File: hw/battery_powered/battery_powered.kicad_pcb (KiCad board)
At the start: 2 copper layers, 69.4 x 54 mm, 10 parts, among them SW101 SKRPABE010, SW102 SKRPABE010, U102 OSL10564-IB, U103 chofutech_logo

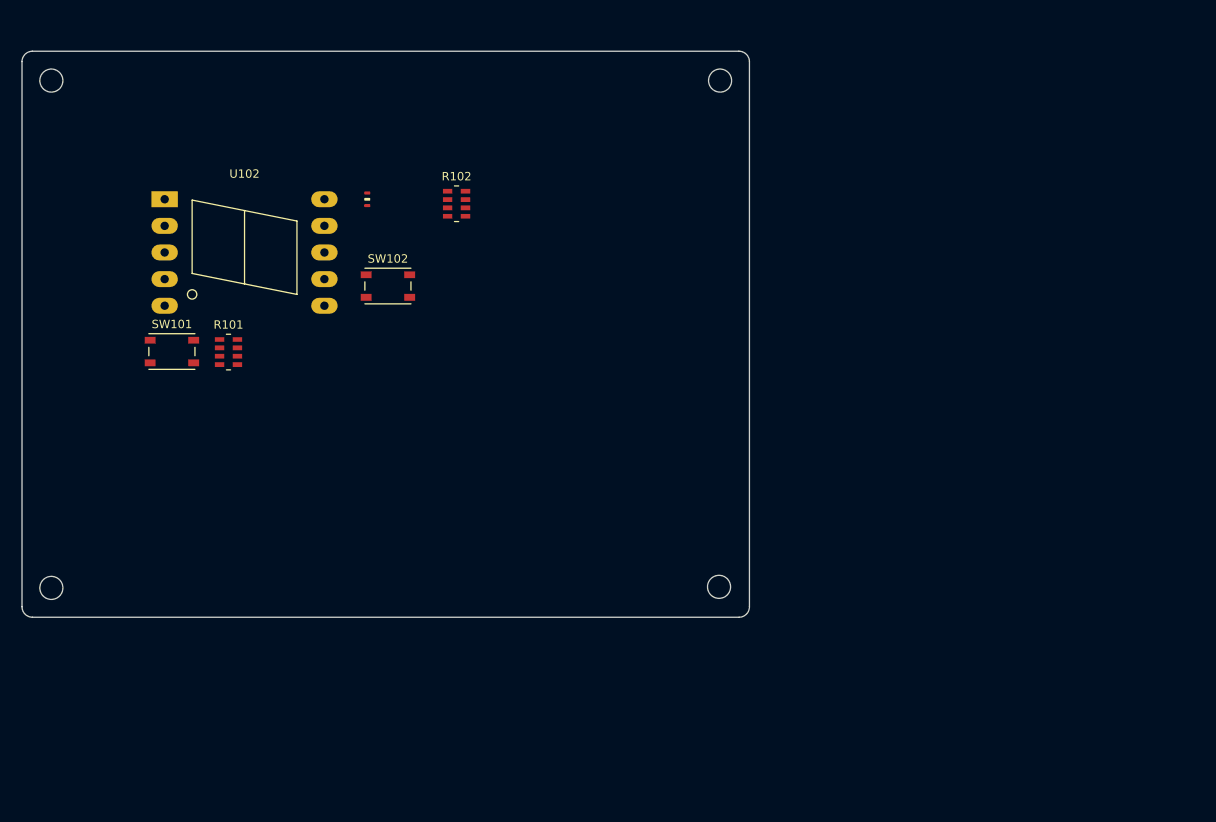
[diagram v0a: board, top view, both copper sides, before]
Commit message: add battery_powered footprints
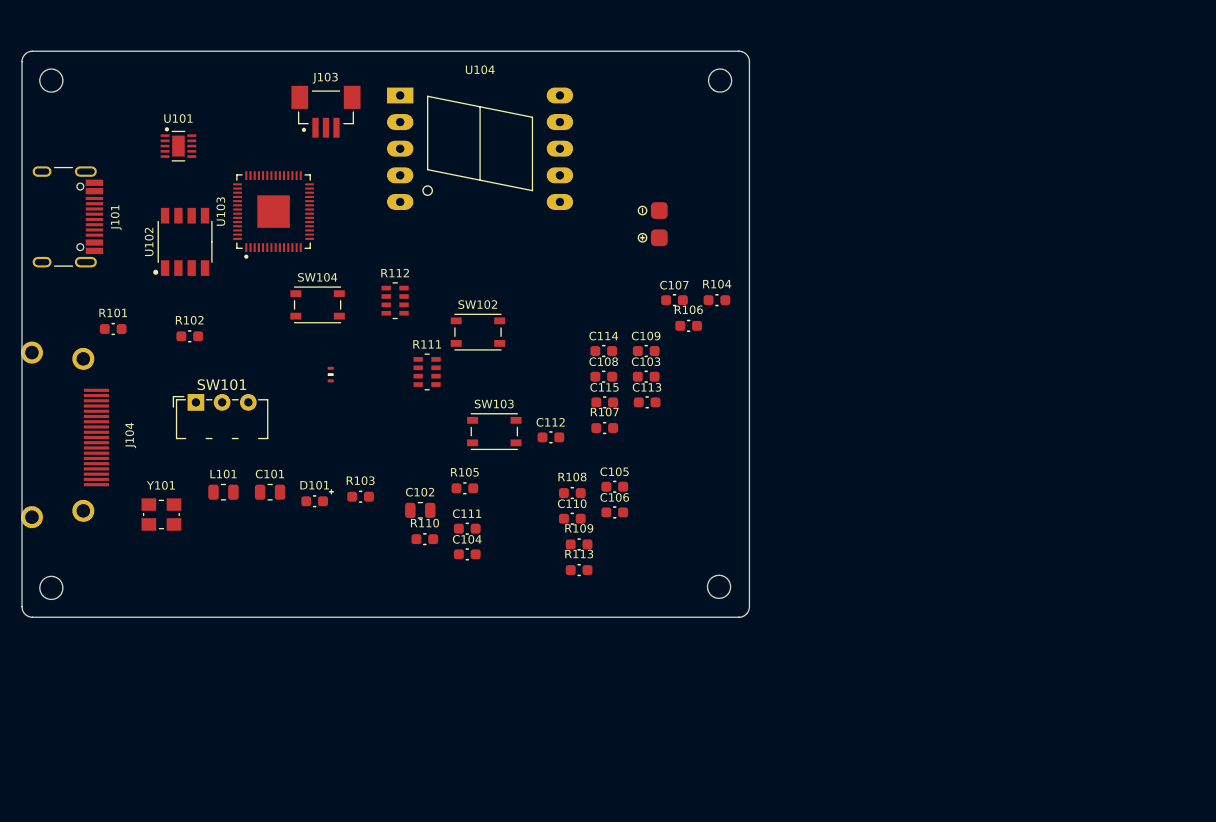
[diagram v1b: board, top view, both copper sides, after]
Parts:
- added C101: C_2012m, 00_custom_lib:C_2012m, F.Cu at (73.7, 92.1)
- added C102: C_2012m, 00_custom_lib:C_2012m, F.Cu at (88.0, 93.8)
- added C103: C_1608m, 00_custom_lib:C_1608m, F.Cu at (109.5, 81.0)
- added C104: C_1608m, 00_custom_lib:C_1608m, F.Cu at (92.5, 98.0)
- added C105: C_1608m, 00_custom_lib:C_1608m, F.Cu at (106.5, 91.5)
- added C106: C_1608m, 00_custom_lib:C_1608m, F.Cu at (106.5, 94.0)
- added C107: C_1608m, 00_custom_lib:C_1608m, F.Cu at (112.2, 73.8)
- added C108: C_1608m, 00_custom_lib:C_1608m, F.Cu at (105.5, 81.0)
- added C109: C_1608m, 00_custom_lib:C_1608m, F.Cu at (109.5, 78.6)
- added C110: C_1608m, 00_custom_lib:C_1608m, F.Cu at (102.5, 94.6)
- added C111: C_1608m, 00_custom_lib:C_1608m, F.Cu at (92.5, 95.5)
- added C112: C_1608m, 00_custom_lib:C_1608m, F.Cu at (100.5, 86.8)
- added C113: C_1608m, 00_custom_lib:C_1608m, F.Cu at (109.6, 83.5)
- added C114: C_1608m, 00_custom_lib:C_1608m, F.Cu at (105.5, 78.6)
- added C115: C_1608m, 00_custom_lib:C_1608m, F.Cu at (105.6, 83.5)
- added D101: SML-E12P8WT86, 00_custom_lib:SML-E12P8WT86, F.Cu at (77.9, 92.9)
- added J101: 5077CR-16SMC2-BK-TR, 00_custom_lib:5077CR-16SMC2-BK-TR_hand, F.Cu at (51.9, 65.8)
- added J102: battery_wire_pad, 00_custom_lib:battery_wire_pad, F.Cu at (110.8, 66.5)
- added J103: BM03B-SRSS-TB(LF)(SN)_pico_debug, 00_custom_lib:BM03B-SRSS-TB(LF)(SN)_hand, F.Cu at (79.0, 55.8)
- added J104: 10029449-111RLF, 00_custom_lib:10029449-111RLF_hand, F.Cu at (57.8, 86.6)
- added L101: DFE201210S-2R2M, 00_custom_lib:DFE201210S-2R2M, F.Cu at (69.2, 92.1)
- added R103: R_1608m, 00_custom_lib:R_1608m, F.Cu at (82.3, 92.5)
- added R104: R_1608m, 00_custom_lib:R_1608m, F.Cu at (116.3, 73.8)
- added R105: R_1608m, 00_custom_lib:R_1608m, F.Cu at (92.2, 91.7)
- added R106: R_1608m, 00_custom_lib:R_1608m, F.Cu at (113.6, 76.2)
- added R107: R_1608m, 00_custom_lib:R_1608m, F.Cu at (105.6, 86.0)
- added R108: R_1608m, 00_custom_lib:R_1608m, F.Cu at (102.5, 92.2)
- added R109: R_1608m, 00_custom_lib:R_1608m, F.Cu at (103.2, 97.0)
- added R110: R_1608m, 00_custom_lib:R_1608m, F.Cu at (88.4, 96.5)
- added R111: 742C083101JP, 00_custom_lib:742C083101JP, F.Cu at (88.7, 80.6)
- added R112: 742C083101JP, 00_custom_lib:742C083101JP, F.Cu at (85.6, 73.8)
- added R113: R_1608m, 00_custom_lib:R_1608m, F.Cu at (103.2, 99.5)
- added SW103: SKRPABE010, 00_custom_lib:SKRPABE010, F.Cu at (95.1, 86.3)
- added SW104: SKRPABE010, 00_custom_lib:SKRPABE010, F.Cu at (78.2, 74.2)
- added U101: RT6150B-33GQW, 00_custom_lib:RT6150B-33GQW, F.Cu at (64.9, 59.0)
- added U104: OSL10564-IB, 00_custom_lib:OSL10564-IB, F.Cu at (86.1, 54.2)
- added U105: chofutech_logo, 00_custom_lib:chofutech_logo_6.6mm, F.Cu at (82.0, 82.8)
- added Y101: FA-238V, 00_custom_lib:FA-238V, F.Cu at (63.3, 94.2)
- R101, R102: value 742C083101JP -> R_1608m; footprint 00_custom_lib:742C083101JP -> 00_custom_lib:R_1608m
- SW101: value SKRPABE010 -> SS12D01G4; footprint 00_custom_lib:SKRPABE010 -> 00_custom_lib:SS12D01G4
- U102: value OSL10564-IB -> W25Q16JVSNIQ; footprint 00_custom_lib:OSL10564-IB -> 00_custom_lib:W25Q16JVSNIQ
- U103: value chofutech_logo -> RP2040; footprint 00_custom_lib:chofutech_logo_6.6mm -> 00_custom_lib:RP2040
- moved R102 28.4 mm to (66.0, 77.2)
- moved U103 11.5 mm to (74.0, 65.3), turned to 90 degrees
- moved R101 11.2 mm to (58.7, 76.5)
- moved SW102 9.65 mm to (93.5, 76.8)
- moved SW101 5.36 mm to (66.6, 83.5)
- moved U102 4.51 mm to (65.6, 68.2), turned to 90 degrees
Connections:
- R101 pad 1: /GPIO9 -> GND
- R101 pad 2: /GPIO8 -> Net-(J101-PadB5)
- R102 pad 1: /GPIO5 -> GND
- R102 pad 2: /GPIO4 -> Net-(J101-PadA5)
- SW101 pad 1: /RUN -> +5VA
- SW101 pad 2: /RUN -> VCC
- SW101 pad 3: GND -> +BATT
- SW102 pad 1: /GPIO10 -> Net-(R107-Pad1)
- SW102 pad 2: /GPIO10 -> Net-(R107-Pad1)
- U102 pad 1: /SEG_E -> /QSPI_SS
- U102 pad 2: /SEG_D -> /QSPI_SD1
- U102 pad 3: +3V3 -> /QSPI_SD2
- U102 pad 4: /SEG_C -> GND
- U102 pad 5: /SEG_DP -> /QSPI_SD0
- U102 pad 6: /SEG_B -> /QSPI_SCLK
- U102 pad 7: /SEG_A -> /QSPI_SD3

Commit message: add DVI output circuit to battery_powered composition
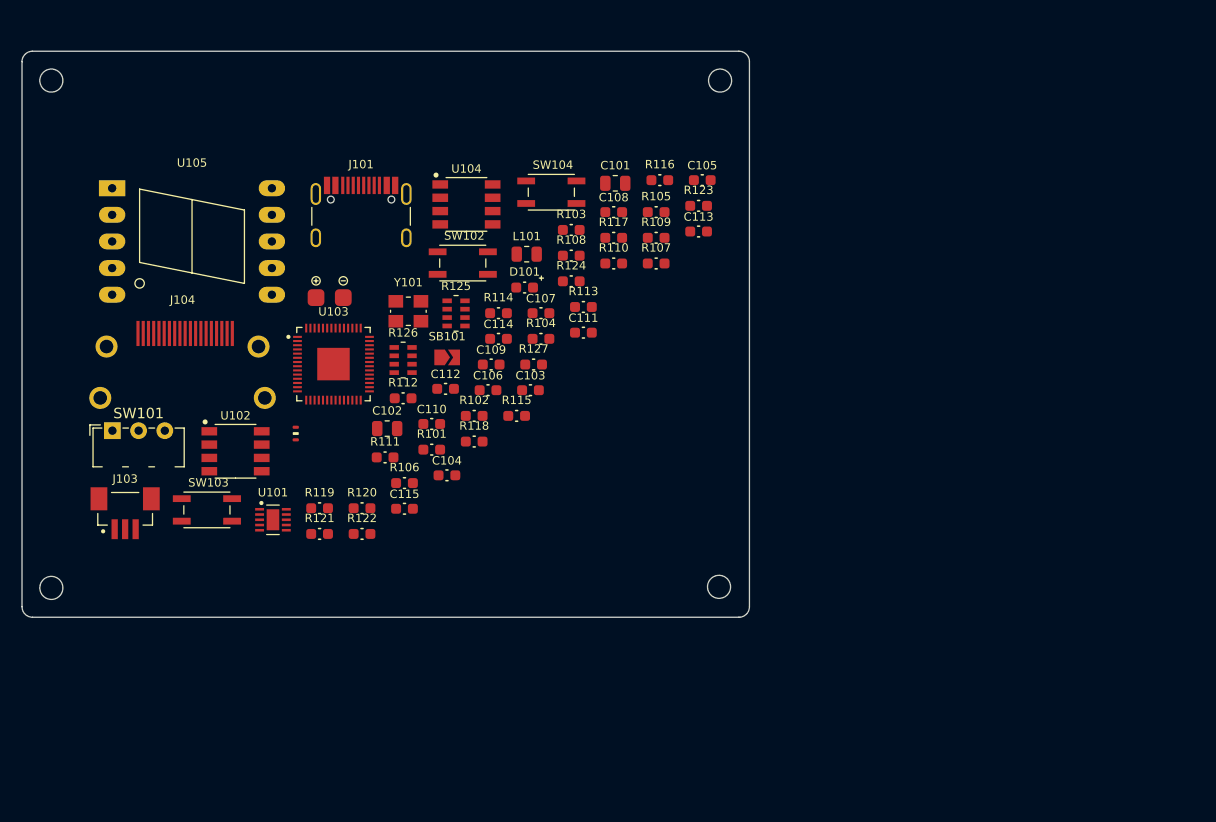
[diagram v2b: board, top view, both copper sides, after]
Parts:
- added R114: R_1608m, 00_custom_lib:R_1608m, F.Cu at (95.5, 75.0)
- added R115: R_1608m, 00_custom_lib:R_1608m, F.Cu at (97.2, 84.8)
- added R116: R_1608m, 00_custom_lib:R_1608m, F.Cu at (110.8, 62.3)
- added R117: R_1608m, 00_custom_lib:R_1608m, F.Cu at (106.5, 67.8)
- added R118: R_1608m, 00_custom_lib:R_1608m, F.Cu at (93.1, 87.2)
- added R119: R_1608m, 00_custom_lib:R_1608m, F.Cu at (78.4, 93.6)
- added R120: R_1608m, 00_custom_lib:R_1608m, F.Cu at (82.4, 93.6)
- added R121: R_1608m, 00_custom_lib:R_1608m, F.Cu at (78.4, 96.0)
- added R122: R_1608m, 00_custom_lib:R_1608m, F.Cu at (82.4, 96.0)
- added R123: R_1608m, 00_custom_lib:R_1608m, F.Cu at (114.5, 64.8)
- added R124: R_1608m, 00_custom_lib:R_1608m, F.Cu at (102.4, 72.0)
- added R125: 742C083101JP, 00_custom_lib:742C083101JP, F.Cu at (91.4, 75.0)
- added R126: 742C083101JP, 00_custom_lib:742C083101JP, F.Cu at (86.4, 79.5)
- added R127: R_1608m, 00_custom_lib:R_1608m, F.Cu at (98.8, 79.9)
- added SB101: jumper_2pole_solder, 00_custom_lib:jumper_2pole_solder, F.Cu at (90.6, 79.2)
- added U106: chofutech_logo, 00_custom_lib:chofutech_logo_6.6mm, F.Cu at (78.7, 88.4)
- R111, R112: value 742C083101JP -> R_1608m; footprint 00_custom_lib:742C083101JP -> 00_custom_lib:R_1608m
- SW102, SW103, SW104: footprint 00_custom_lib:SKRPABE010 -> 00_custom_lib:SKRPABE010_hand
- U104: value OSL10564-IB -> PCA9306D; footprint 00_custom_lib:OSL10564-IB -> 00_custom_lib:PCA9306D
- U105: value chofutech_logo -> OSL10564-IB; footprint 00_custom_lib:chofutech_logo_6.6mm -> 00_custom_lib:OSL10564-IB
- moved C101 44.2 mm to (106.6, 62.6)
- moved J103 42.8 mm to (59.8, 94.1)
- moved L101 36.8 mm to (98.2, 69.4)
- moved U101 36.8 mm to (73.9, 94.7)
- moved R101 32.5 mm to (89.1, 88.0)
- moved R103 32.4 mm to (102.4, 67.0)
- moved J102 32.2 mm to (79.3, 73.5), turned to 0 degrees
- moved R105 32.1 mm to (110.5, 65.3)
- moved R110 31.9 mm to (106.5, 70.2)
- moved R106 31.0 mm to (86.5, 91.2)
- moved U105 30.6 mm to (58.6, 63.1)
- moved Y101 30.5 mm to (86.9, 74.8)
- moved J101 30.5 mm to (82.3, 67.8), turned to 0 degrees
- moved C105 30.4 mm to (114.9, 62.3)
- moved R109 30.2 mm to (110.5, 67.8)
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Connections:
- J104 pad 1: unconnected-(J104-Pad1) -> Net-(J104-Pad1)
- J104 pad 10: unconnected-(J104-Pad10) -> Net-(J104-Pad10)
- J104 pad 11: unconnected-(J104-Pad11) -> GND
- J104 pad 12: unconnected-(J104-Pad12) -> Net-(J104-Pad12)
- J104 pad 15: unconnected-(J104-Pad15) -> Net-(J104-Pad15)
- J104 pad 16: unconnected-(J104-Pad16) -> Net-(J104-Pad16)
- J104 pad 17: unconnected-(J104-Pad17) -> GND
- J104 pad 18: unconnected-(J104-Pad18) -> Net-(J104-Pad18)
- J104 pad 19: unconnected-(J104-Pad19) -> Net-(J104-Pad19)
- J104 pad 2: unconnected-(J104-Pad2) -> GND
- J104 pad 3: unconnected-(J104-Pad3) -> Net-(J104-Pad3)
- J104 pad 4: unconnected-(J104-Pad4) -> Net-(J104-Pad4)
- J104 pad 5: unconnected-(J104-Pad5) -> GND
- J104 pad 6: unconnected-(J104-Pad6) -> Net-(J104-Pad6)
- J104 pad 7: unconnected-(J104-Pad7) -> Net-(J104-Pad7)
- J104 pad 8: unconnected-(J104-Pad8) -> GND
- J104 pad 9: unconnected-(J104-Pad9) -> Net-(J104-Pad9)
- R111 pad 1: /GPIO9 -> Net-(J104-Pad1)
- R111 pad 2: /GPIO8 -> /DVI_D2+
- R112 pad 1: /GPIO5 -> Net-(J104-Pad3)
- R112 pad 2: /GPIO4 -> /DVI_D2-
- R113 pad 1: /GPIO25 -> Net-(J104-Pad4)
- R113 pad 2: Net-(D101-Pad2) -> /DVI_D1+
- U103 pad 14: unconnected-(U103-Pad14) -> /DVI_HPD
- U103 pad 15: unconnected-(U103-Pad15) -> /DVI_D0+
- U103 pad 16: unconnected-(U103-Pad16) -> /DVI_D0-
- U103 pad 17: unconnected-(U103-Pad17) -> /DVI_CK+
- U103 pad 18: unconnected-(U103-Pad18) -> /DVI_CK-
- U103 pad 27: unconnected-(U103-Pad27) -> /DVI_D2+
- U103 pad 28: unconnected-(U103-Pad28) -> /DVI_D2-
- U103 pad 29: unconnected-(U103-Pad29) -> /DVI_D1+
- U103 pad 30: unconnected-(U103-Pad30) -> /DVI_D1-
- U103 pad 31: unconnected-(U103-Pad31) -> /DVI_SDA
- U103 pad 32: unconnected-(U103-Pad32) -> /DVI_SCL
- U104 pad 1: /SEG_E -> GND
- U104 pad 2: /SEG_D -> +3V3
- U104 pad 3: +3V3 -> /DVI_SCL
- U104 pad 4: /SEG_C -> /DVI_SDA
- U104 pad 5: /SEG_DP -> Net-(J104-Pad16)
- U104 pad 6: /SEG_B -> Net-(J104-Pad15)
- U104 pad 7: /SEG_A -> +5VA
- U104 pad 8: +3V3 -> +5VA

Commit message: change DVI pin assignment (PicoDVI cfg written in schematic)
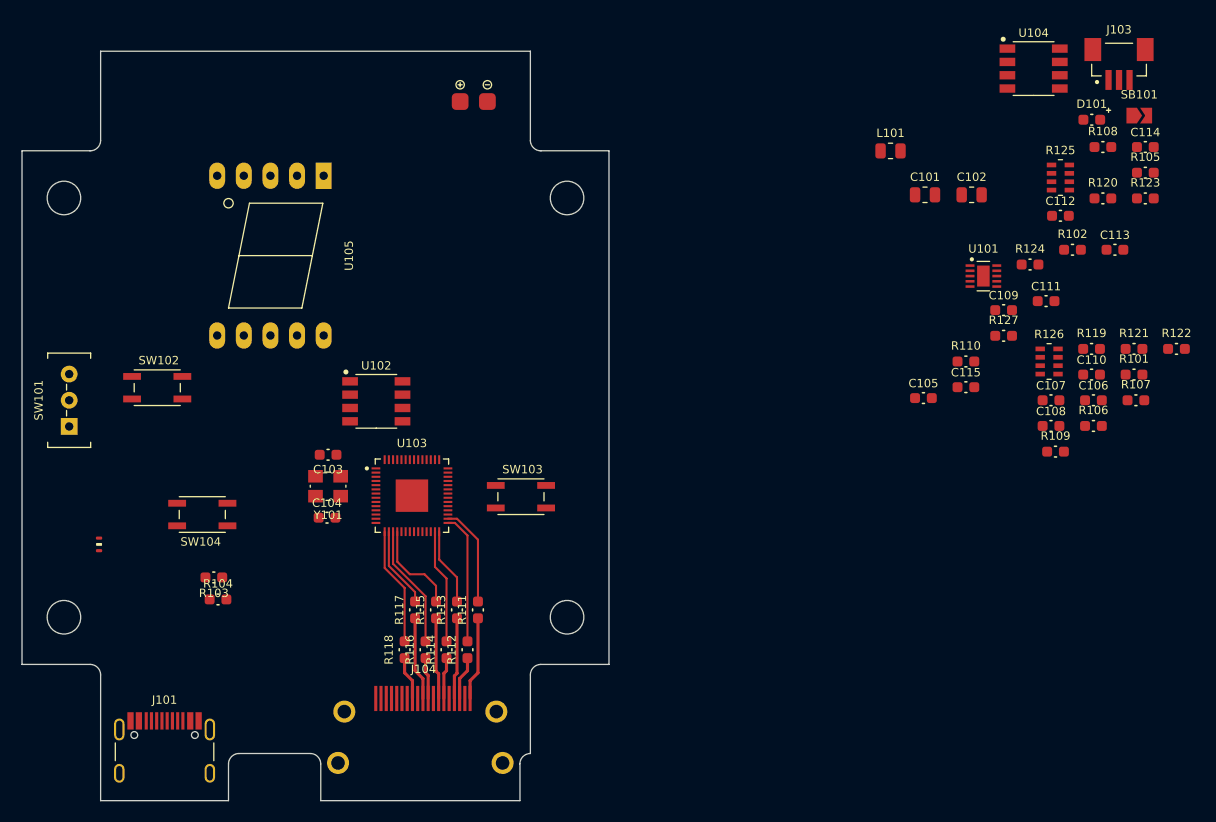
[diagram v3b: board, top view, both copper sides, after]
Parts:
- H101, H102, H103, H104: footprint 00_custom_lib:MountingHole_2.2mm_M2 -> 00_custom_lib:MountingHole_3.2mm_M3
- moved J103 104.1 mm to (154.7, 51.2)
- moved H104 80.9 mm to (54.0, 104.0), turned to 180 degrees
- moved R121 79.7 mm to (156.1, 78.4)
- moved R122 79.7 mm to (160.1, 78.4)
- moved R120 76.6 mm to (153.1, 64.0)
- moved R119 75.2 mm to (152.0, 78.4)
- moved H103 72.7 mm to (54.0, 64.0), turned to 180 degrees
- moved U101 71.7 mm to (141.7, 71.5)
- moved H101 71.0 mm to (102.0, 104.0), turned to 180 degrees
- moved SB101 69.9 mm to (156.6, 56.1)
- moved R101 67.4 mm to (156.1, 80.8)
- moved R106 66.0 mm to (152.2, 85.8)
- moved C114 64.4 mm to (157.2, 59.1)
- moved C110 63.1 mm to (152.0, 80.8)
- moved H102 61.7 mm to (102.0, 64.0), turned to 180 degrees
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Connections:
- U103 pad 15: /DVI_D0+ -> /DVI_CK-
- U103 pad 16: /DVI_D0- -> /DVI_CK+
- U103 pad 17: /DVI_CK+ -> /DVI_D0-
- U103 pad 18: /DVI_CK- -> /DVI_D0+
- U103 pad 27: /DVI_D2+ -> /DVI_D1-
- U103 pad 28: /DVI_D2- -> /DVI_D1+
- U103 pad 29: /DVI_D1+ -> /DVI_D2-
- U103 pad 30: /DVI_D1- -> /DVI_D2+
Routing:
- net /DVI_D2-: track 0.00 -> 12.5 mm
- net /DVI_D0-: track 0.00 -> 11.7 mm
- net /DVI_CK-: track 0.00 -> 11.3 mm
- net /DVI_D1-: track 0.00 -> 10.9 mm
- net /DVI_D2+: track 0.00 -> 9.59 mm
- net /DVI_D0+: track 0.00 -> 9.02 mm
- net Net-(J104-Pad10): track 0.00 -> 7.96 mm
- net Net-(J104-Pad1): track 0.00 -> 7.96 mm
- net Net-(J104-Pad7): track 0.00 -> 7.75 mm
- net Net-(J104-Pad4): track 0.00 -> 7.75 mm
- net /DVI_CK+: track 0.00 -> 7.70 mm
- net /DVI_D1+: track 0.00 -> 7.37 mm
- net Net-(J104-Pad3): track 0.00 -> 4.16 mm
- net Net-(J104-Pad12): track 0.00 -> 4.16 mm
- net Net-(J104-Pad9): track 0.00 -> 3.95 mm
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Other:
- board size 69.4 x 54 mm -> 56 x 71.5 mm
